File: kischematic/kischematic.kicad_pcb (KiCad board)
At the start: 2 copper layers, 26.7 x 50 mm, 104 parts, among them IC1 BlueNRG, IC10 128x64OLED, IC2 EFM32ZG108, IC3 BQ297xx, IC4 AAT3672IWO-4.2-1, IC5 TPS6223xx, IC6 APDS-9303, IC7 APDS-9303, IC8 BSD840NH6327XTSA1, IC9 MMA8653FC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

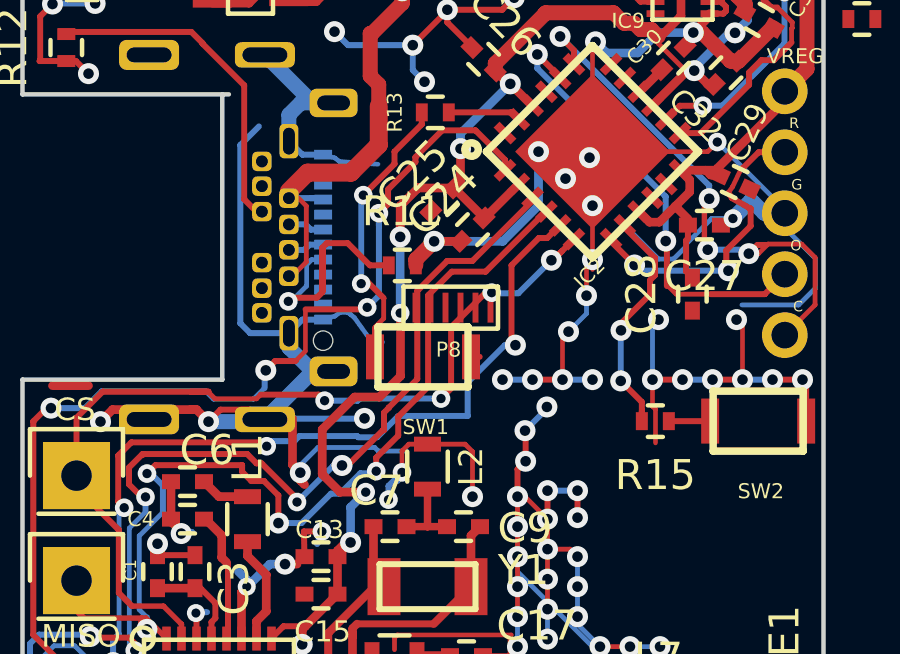
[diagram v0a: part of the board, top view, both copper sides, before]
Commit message: Some significant progress on display connector routing.
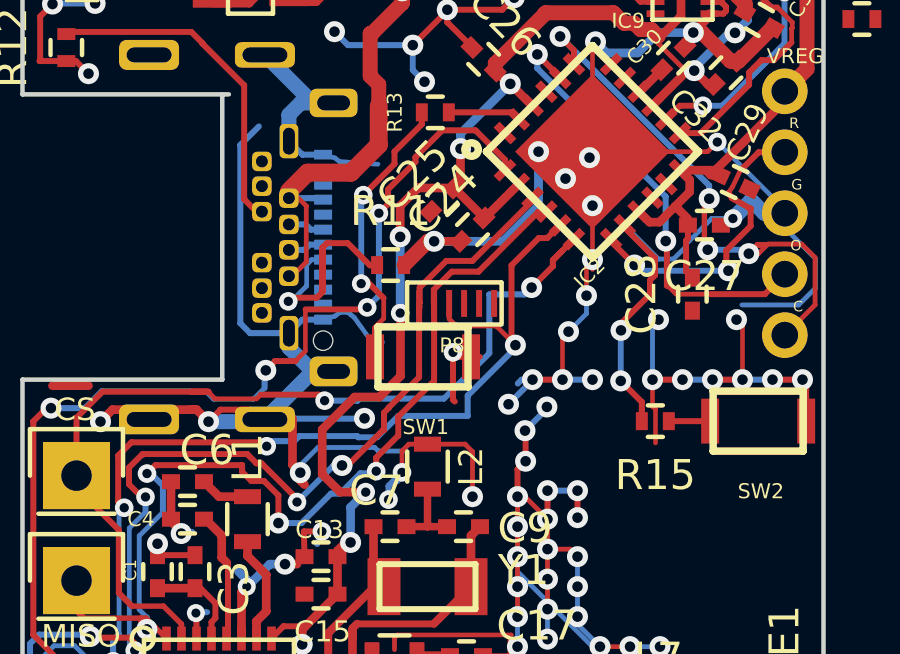
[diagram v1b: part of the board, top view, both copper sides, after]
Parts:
- moved R11 0.39 mm to (88.3, 49.8)
- moved P8 0.18 mm to (90.2, 51.1)
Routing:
- net GND: track 450.8 -> 454.1 mm, vias 161 -> 162
- net SPI_CLK: track 46.2 -> 49.1 mm
- net BNRG_SPI_CS: track 31.1 -> 31.2 mm, vias 4 -> 2

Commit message: Minor.
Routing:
- net GND: track 454.1 -> 451.7 mm, vias 162 -> 161
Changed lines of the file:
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@@
     (thickness 1.6)
     (drawings 22)
-    (tracks 1893)
+    (tracks 1890)
     (zones 0)
     (modules 104)
@@
   (segment (start 88.65 56.69) (end 88.2 57.14) (width 0.2) (layer B.Cu) (net 1))
   (segment (start 88.2 57.14) (end 88.2 57.6) (width 0.2) (layer B.Cu) (net 1))
-  (via (at 87.4 54.89) (size 0.7) (drill 0.35) (layers F.Cu B.Cu) (net 1))
-  (segment (start 85 54.9) (end 87.39 54.9) (width 0.2) (layer B.Cu) (net 1) (status 10))
-  (segment (start 87.39 54.9) (end 87.4 54.89) (width 0.2) (layer B.Cu) (net 1))
   (via (at 93 53.6) (size 0.7) (drill 0.35) (layers F.Cu B.Cu) (net 1))
   (segment (start 93 53.6) (end 94 53.6) (width 0.2) (layer F.Cu) (net 1))

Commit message: Some possible small steps of routing progress.
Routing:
- net VREG: track 202.1 -> 203.3 mm, vias 18 -> 20
- net BNRG_SPI_IRQ: track 48.9 -> 49.9 mm

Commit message: More routing tweaks.
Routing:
- net VREG: track 203.3 -> 203.9 mm, vias 20 -> 21
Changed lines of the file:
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@@
     (thickness 1.6)
     (drawings 22)
-    (tracks 1905)
+    (tracks 1911)
     (zones 0)
     (modules 104)
@@
   )
   (setup
-    (last_trace_width 0.16)
+    (last_trace_width 0.29)
     (user_trace_width 0.16)
     (user_trace_width 0.2)
@@
   (segment (start 94.92 44.11) (end 95.89 45.08) (width 0.2) (layer F.Cu) (net 1) (status 30))
   (segment (start 94 47) (end 95 48) (width 0.2) (layer F.Cu) (net 1) (status 30))
+  (segment (start 92.26 43.74) (end 92.26 43.7) (width 0.29) (layer B.Cu) (net 2))
+  (segment (start 92.26 43.7) (end 92.15 43.59) (width 0.29) (layer B.Cu) (net 2))
+  (segment (start 92.56 44) (end 92.2 43.64) (width 0.29) (layer B.Cu) (net 2))
+  (segment (start 92.15 43.59) (end 92.2 43.64) (width 0.29) (layer B.Cu) (net 2))
+  (segment (start 91.76 43.06) (end 92.15 42.67) (width 0.5) (layer F.Cu) (net 2))
+  (segment (start 92.15 42.67) (end 93.41 41.41) (width 0.5) (layer F.Cu) (net 2))
+  (segment (start 92.15 43.59) (end 92.15 42.67) (width 0.29) (layer B.Cu) (net 2))
+  (via (at 92.15 42.67) (size 0.62) (drill 0.31) (layers F.Cu B.Cu) (net 2))
+  (segment (start 93.002423 44.462043) (end 93.002423 44.442423) (width 0.29) (layer F.Cu) (net 2))
+  (segment (start 93.002423 44.442423) (end 92.56 44) (width 0.29) (layer F.Cu) (net 2))
+  (via (at 92.56 44) (size 0.62) (drill 0.31) (layers F.Cu B.Cu) (net 2))
   (via (at 90.65 45.45) (size 0.7) (drill 0.35) (layers F.Cu B.Cu) (net 2))
   (segment (start 90.65 45.45) (end 90.65 46.95) (width 0.29) (layer F.Cu) (net 2))
@@
   (segment (start 91.76 43.31) (end 91.76 43.06) (width 0.5) (layer F.Cu) (net 2) (status 30))
   (segment (start 93.41 41.41) (end 93.41 41.4) (width 0.5) (layer F.Cu) (net 2))
-  (segment (start 91.76 43.06) (end 93.41 41.41) (width 0.5) (layer F.Cu) (net 2) (status 10))
   (segment (start 96.05 41.72) (end 96.39 41.72) (width 0.5) (layer F.Cu) (net 2))
   (segment (start 93.41 41.4) (end 93.44 41.37) (width 0.5) (layer F.Cu) (net 2))
@@
   (segment (start 88 66.76) (end 88 67.2) (width 0.29) (layer F.Cu) (net 2))
   (segment (start 86.5 65.75) (end 86.99 65.75) (width 0.29) (layer F.Cu) (net 2))
-  (via (at 92.26 43.74) (size 0.7) (drill 0.35) (layers F.Cu B.Cu) (net 2))
   (segment (start 76.94 29.49) (end 76.8 29.63) (width 0.45) (layer F.Cu) (net 2))
   (segment (start 76.8 29.63) (end 76.8 31.175) (width 0.45) (layer F.Cu) (net 2))
@@
   (segment (start 98.938124 46.77756) (end 98.779282 46.618718) (width 0.29) (layer F.Cu) (net 2) (status 10))
   (via (at 99.75 42.04) (size 0.7) (drill 0.35) (layers F.Cu B.Cu) (net 2))
-  (segment (start 92.26 43.74) (end 92.19 43.74) (width 0.29) (layer F.Cu) (net 2))
-  (segment (start 92.19 43.74) (end 91.76 43.31) (width 0.29) (layer F.Cu) (net 2) (status 20))
   (segment (start 98.9 40.6) (end 99.55 40.6) (width 0.2) (layer F.Cu) (net 2) (status 30))
   (segment (start 99.55 40.6) (end 99.8 40.35) (width 0.2) (layer F.Cu) (net 2) (status 30))
@@
   (segment (start 97.916815 46.618718) (end 98.779282 46.618718) (width 0.29) (layer F.Cu) (net 2) (status 10))
   (segment (start 93.002423 44.462043) (end 92.982043 44.462043) (width 0.29) (layer F.Cu) (net 2) (status 30))
-  (segment (start 92.982043 44.462043) (end 92.26 43.74) (width 0.29) (layer F.Cu) (net 2) (status 10))
   (via (at 87.44 57.35) (size 0.62) (drill 0.31) (layers F.Cu B.Cu) (net 2))
   (segment (start 87.44 57.35) (end 86.59 57.35) (width 0.29) (layer F.Cu) (net 2))

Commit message: Some further routing tweaks.
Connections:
- IC2 pad 21: DISPLAY_CS -> MAINBUTTON
- IC2 pad 23: MAINBUTTON -> DISPLAY_CS
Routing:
- net DISPLAY_CS: track 0.01 -> 3.18 mm
- net MAINBUTTON: track 2.43 -> 4.07 mm
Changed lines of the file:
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@@
     (thickness 1.6)
     (drawings 22)
-    (tracks 1911)
+    (tracks 1920)
     (zones 0)
     (modules 104)
@@
   )
   (setup
-    (last_trace_width 0.29)
+    (last_trace_width 0.2)
     (user_trace_width 0.16)
     (user_trace_width 0.2)
@@
       (net 39 SWDIO))
     (pad 21 smd rect (at 0.325 -2.5 135) (size 0.8 0.28) (layers F.Cu F.Paste F.Mask)
-      (net 106 DISPLAY_CS))
+      (net 70 MAINBUTTON))
     (pad 22 smd rect (at -0.325 -2.5 135) (size 0.8 0.28) (layers F.Cu F.Paste F.Mask)
       (net 2 VREG))
     (pad 23 smd rect (at -0.975 -2.5 135) (size 0.8 0.28) (layers F.Cu F.Paste F.Mask)
-      (net 70 MAINBUTTON))
+      (net 106 DISPLAY_CS))
     (pad 24 smd rect (at -1.625 -2.499999 135) (size 0.8 0.28) (layers F.Cu F.Paste F.Mask)
       (net 105 DISPLAY_RESET))
@@
   (segment (start 94.92 44.11) (end 95.89 45.08) (width 0.2) (layer F.Cu) (net 1) (status 30))
   (segment (start 94 47) (end 95 48) (width 0.2) (layer F.Cu) (net 1) (status 30))
+  (via (at 92.58 44.05) (size 0.62) (drill 0.31) (layers F.Cu B.Cu) (net 2))
+  (segment (start 92.58 44.05) (end 92.58 44.02) (width 0.29) (layer B.Cu) (net 2))
+  (segment (start 92.58 44.02) (end 92.15 43.59) (width 0.29) (layer B.Cu) (net 2))
+  (segment (start 92.58 44.05) (end 92.59038 44.05) (width 0.29) (layer F.Cu) (net 2))
+  (segment (start 92.59038 44.05) (end 93.002423 44.462043) (width 0.29) (layer F.Cu) (net 2))
   (segment (start 92.26 43.74) (end 92.26 43.7) (width 0.29) (layer B.Cu) (net 2))
   (segment (start 92.26 43.7) (end 92.15 43.59) (width 0.29) (layer B.Cu) (net 2))
-  (segment (start 92.56 44) (end 92.2 43.64) (width 0.29) (layer B.Cu) (net 2))
-  (segment (start 92.15 43.59) (end 92.2 43.64) (width 0.29) (layer B.Cu) (net 2))
   (segment (start 91.76 43.06) (end 92.15 42.67) (width 0.5) (layer F.Cu) (net 2))
   (segment (start 92.15 42.67) (end 93.41 41.41) (width 0.5) (layer F.Cu) (net 2))
   (segment (start 92.15 43.59) (end 92.15 42.67) (width 0.29) (layer B.Cu) (net 2))
   (via (at 92.15 42.67) (size 0.62) (drill 0.31) (layers F.Cu B.Cu) (net 2))
-  (segment (start 93.002423 44.462043) (end 93.002423 44.442423) (width 0.29) (layer F.Cu) (net 2))
-  (segment (start 93.002423 44.442423) (end 92.56 44) (width 0.29) (layer F.Cu) (net 2))
-  (via (at 92.56 44) (size 0.62) (drill 0.31) (layers F.Cu B.Cu) (net 2))
   (via (at 90.65 45.45) (size 0.7) (drill 0.35) (layers F.Cu B.Cu) (net 2))
   (segment (start 90.65 45.45) (end 90.65 46.95) (width 0.29) (layer F.Cu) (net 2))
@@
   (segment (start 86.84 49.05) (end 86.15 49.05) (width 0.2) (layer F.Cu) (net 69))
   (segment (start 87.58 49.79) (end 86.84 49.05) (width 0.2) (layer F.Cu) (net 69))
-  (segment (start 92.521662 44.921662) (end 92.29 44.69) (width 0.2) (layer F.Cu) (net 70) (status 30))
-  (segment (start 92.29 44.69) (end 90.21 44.69) (width 0.2) (layer F.Cu) (net 70) (status 30))
-  (segment (start 92.542804 44.921662) (end 92.521662 44.921662) (width 0.2) (layer F.Cu) (net 70) (status 30))
+  (segment (start 92.46 43.37) (end 92.82962 43.37) (width 0.16) (layer F.Cu) (net 70))
+  (segment (start 92.82962 43.37) (end 93.462043 44.002423) (width 0.16) (layer F.Cu) (net 70))
+  (segment (start 91.79 44.04) (end 92.46 43.37) (width 0.16) (layer F.Cu) (net 70))
+  (segment (start 90.99 44.04) (end 91.79 44.04) (width 0.16) (layer F.Cu) (net 70))
+  (segment (start 90.34 44.69) (end 90.99 44.04) (width 0.2) (layer F.Cu) (net 70))
+  (segment (start 90.21 44.69) (end 90.34 44.69) (width 0.2) (layer F.Cu) (net 70))
+  (segment (start 93.452423 44.002423) (end 93.462043 44.002423) (width 0.2) (layer F.Cu) (net 70) (status 30))
   (segment (start 88.04 51.56) (end 88.04 50.9) (width 0.16) (layer F.Cu) (net 71))
   (segment (start 88.04 50.9) (end 88.05 50.89) (width 0.16) (layer F.Cu) (net 71))
@@
   (segment (start 83.9 40.7) (end 83.9 39.8) (width 0.29) (layer F.Cu) (net 102))
   (segment (start 83.95 39.75) (end 84.875 39.75) (width 0.29) (layer F.Cu) (net 102) (status 20))
-  (segment (start 93.452423 44.002423) (end 93.462043 44.002423) (width 0.2) (layer F.Cu) (net 106) (status 30))
+  (segment (start 91.34 44.84) (end 91.34 46.57) (width 0.2) (layer F.Cu) (net 106))
+  (segment (start 91.56 44.62) (end 91.34 44.84) (width 0.2) (layer F.Cu) (net 106))
+  (segment (start 92.26 44.62) (end 91.56 44.62) (width 0.2) (layer F.Cu) (net 106))
+  (segment (start 92.542804 44.902804) (end 92.26 44.62) (width 0.2) (layer F.Cu) (net 106))
+  (segment (start 92.542804 44.921662) (end 92.542804 44.902804) (width 0.2) (layer F.Cu) (net 106))
+  (segment (start 92.542804 44.921662) (end 92.521662 44.921662) (width 0.2) (layer F.Cu) (net 106) (status 30))
   (zone (net 1) (net_name GND) (layer F.Cu) (hatch edge 0.508)
     (connect_pads (clearance 0.18))

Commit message: More routing tweaks.
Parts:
- moved R13 0.30 mm to (89.8, 44.4)
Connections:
- IC2 pad 1: BNRG_SPI_IRQ -> DISPLAY_CS
- IC2 pad 23: DISPLAY_CS -> BNRG_SPI_IRQ
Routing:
- net DISPLAY_CS: track 3.18 -> 0.01 mm
- net BNRG_SPI_IRQ: track 49.9 -> 49.1 mm
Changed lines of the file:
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@@
     (thickness 1.6)
     (drawings 22)
-    (tracks 1920)
+    (tracks 1912)
     (zones 0)
     (modules 104)
@@
   )
   (setup
-    (last_trace_width 0.2)
+    (last_trace_width 0.16)
     (user_trace_width 0.16)
     (user_trace_width 0.2)
@@
       (net 2 VREG))
     (pad 23 smd rect (at -0.975 -2.5 135) (size 0.8 0.28) (layers F.Cu F.Paste F.Mask)
-      (net 106 DISPLAY_CS))
+      (net 28 BNRG_SPI_IRQ))
     (pad 24 smd rect (at -1.625 -2.499999 135) (size 0.8 0.28) (layers F.Cu F.Paste F.Mask)
       (net 105 DISPLAY_RESET))
@@
       (net 2 VREG))
     (pad 1 smd rect (at -2.499999 -1.625 45) (size 0.8 0.28) (layers F.Cu F.Paste F.Mask)
-      (net 28 BNRG_SPI_IRQ))
+      (net 106 DISPLAY_CS))
   )
   (module Capacitors_SMD:C_0402 (layer F.Cu)
@@
   )
   (module Resistors_SMD:R_0402 (layer F.Cu)
-    (at 89.76 44.69)
+    (at 89.79 44.39)
     (descr "Resistor SMD 0402, reflow soldering, Vishay (see dcrcw.pdf)")
     (tags "resistor 0402")
@@
   (segment (start 89.01 42.45) (end 89.01 43.28) (width 0.2) (layer B.Cu) (net 1))
   (segment (start 89.01 43.28) (end 89.4 43.67) (width 0.2) (layer B.Cu) (net 1))
-  (via (at 89.4 43.67) (size 0.7) (drill 0.35) (layers F.Cu B.Cu) (net 1))
+  (via (at 89.36 43.46) (size 0.7) (drill 0.35) (layers F.Cu B.Cu) (net 1))
   (segment (start 90.16 41.27) (end 90.16 41.3) (width 0.2) (layer F.Cu) (net 1))
   (segment (start 90.16 41.3) (end 89.01 42.45) (width 0.2) (layer F.Cu) (net 1))
@@
   (segment (start 94.92 44.11) (end 95.89 45.08) (width 0.2) (layer F.Cu) (net 1) (status 30))
   (segment (start 94 47) (end 95 48) (width 0.2) (layer F.Cu) (net 1) (status 30))
+  (via (at 90.65 45.52) (size 0.7) (drill 0.35) (layers F.Cu B.Cu) (net 2))
+  (segment (start 90.65 45.52) (end 90.65 46.95) (width 0.29) (layer F.Cu) (net 2))
+  (segment (start 90.65 46.95) (end 90.388909 47.211091) (width 0.29) (layer F.Cu) (net 2))
+  (segment (start 90.65 45.52) (end 90.65 45.35) (width 0.29) (layer B.Cu) (net 2))
+  (segment (start 90.65 45.35) (end 92.26 43.74) (width 0.29) (layer B.Cu) (net 2))
+  (segment (start 92.26 43.74) (end 92.26 43.7) (width 0.29) (layer B.Cu) (net 2))
+  (segment (start 92.26 43.7) (end 92.15 43.59) (width 0.29) (layer B.Cu) (net 2))
   (via (at 92.58 44.05) (size 0.62) (drill 0.31) (layers F.Cu B.Cu) (net 2))
   (segment (start 92.58 44.05) (end 92.58 44.02) (width 0.29) (layer B.Cu) (net 2))
@@
   (segment (start 92.58 44.05) (end 92.59038 44.05) (width 0.29) (layer F.Cu) (net 2))
   (segment (start 92.59038 44.05) (end 93.002423 44.462043) (width 0.29) (layer F.Cu) (net 2))
-  (segment (start 92.26 43.74) (end 92.26 43.7) (width 0.29) (layer B.Cu) (net 2))
-  (segment (start 92.26 43.7) (end 92.15 43.59) (width 0.29) (layer B.Cu) (net 2))
   (segment (start 91.76 43.06) (end 92.15 42.67) (width 0.5) (layer F.Cu) (net 2))
   (segment (start 92.15 42.67) (end 93.41 41.41) (width 0.5) (layer F.Cu) (net 2))
   (segment (start 92.15 43.59) (end 92.15 42.67) (width 0.29) (layer B.Cu) (net 2))
   (via (at 92.15 42.67) (size 0.62) (drill 0.31) (layers F.Cu B.Cu) (net 2))
-  (via (at 90.65 45.45) (size 0.7) (drill 0.35) (layers F.Cu B.Cu) (net 2))
-  (segment (start 90.65 45.45) (end 90.65 46.95) (width 0.29) (layer F.Cu) (net 2))
-  (segment (start 90.65 46.95) (end 90.388909 47.211091) (width 0.29) (layer F.Cu) (net 2))
-  (segment (start 90.65 45.45) (end 90.65 45.35) (width 0.29) (layer B.Cu) (net 2))
-  (segment (start 90.65 45.35) (end 92.26 43.74) (width 0.29) (layer B.Cu) (net 2))
   (via (at 88.59 48.54) (size 0.62) (drill 0.31) (layers F.Cu B.Cu) (net 2))
   (segment (start 88.59 48.54) (end 88.59 51.38) (width 0.29) (layer B.Cu) (net 2))
@@
   (segment (start 93 64.8) (end 93 66.25) (width 1.2) (layer F.Cu) (net 25) (status 30))
   (segment (start 89.15 62.8) (end 90.25 62.8) (width 0.29) (layer F.Cu) (net 26) (status 30))
-  (segment (start 91.33 47.55) (end 90.86 48.02) (width 0.16) (layer F.Cu) (net 28))
-  (segment (start 90.86 48.02) (end 90.42 48.02) (width 0.16) (layer F.Cu) (net 28))
-  (segment (start 90.42 48.02) (end 89.74 47.34) (width 0.16) (layer F.Cu) (net 28))
-  (segment (start 89.74 47.34) (end 89.54 47.34) (width 0.16) (layer F.Cu) (net 28))
-  (segment (start 89.54 47.34) (end 88.98 47.9) (width 0.16) (layer F.Cu) (net 28))
-  (segment (start 88.98 47.9) (end 88.98 48.14) (width 0.16) (layer F.Cu) (net 28))
-  (segment (start 88.98 48.14) (end 89.14 48.3) (width 0.16) (layer F.Cu) (net 28))
-  (segment (start 87.880813 48.740813) (end 87.880813 48.052123) (width 0.16) (layer F.Cu) (net 28))
-  (segment (start 89.14 48.3) (end 89.14 48.78) (width 0.16) (layer F.Cu) (net 28))
-  (segment (start 89.14 48.78) (end 88.75 49.17) (width 0.16) (layer F.Cu) (net 28))
-  (segment (start 88.75 49.17) (end 88.31 49.17) (width 0.16) (layer F.Cu) (net 28))
-  (segment (start 88.31 49.17) (end 87.880813 48.740813) (width 0.16) (layer F.Cu) (net 28))
-  (segment (start 91.33 47.36) (end 91.33 47.55) (width 0.2) (layer F.Cu) (net 28))
-  (segment (start 92.071282 46.618718) (end 91.33 47.36) (width 0.2) (layer F.Cu) (net 28))
-  (segment (start 92.083185 46.618718) (end 92.071282 46.618718) (width 0.2) (layer F.Cu) (net 28))
+  (segment (start 92.542804 44.921662) (end 92.542804 44.912804) (width 0.16) (layer F.Cu) (net 28))
+  (segment (start 92.542804 44.912804) (end 92.17 44.54) (width 0.16) (layer F.Cu) (net 28))
+  (segment (start 92.17 44.54) (end 90.98 44.54) (width 0.16) (layer F.Cu) (net 28))
+  (segment (start 90.98 44.54) (end 90.58 44.94) (width 0.16) (layer F.Cu) (net 28))
+  (segment (start 88.87 46.34) (end 88.87 46.71) (width 0.16) (layer F.Cu) (net 28))
+  (segment (start 90.58 44.94) (end 90.27 44.94) (width 0.16) (layer F.Cu) (net 28))
+  (segment (start 90.27 44.94) (end 88.87 46.34) (width 0.16) (layer F.Cu) (net 28))
+  (segment (start 88.87 46.71) (end 87.880813 47.699187) (width 0.16) (layer F.Cu) (net 28))
+  (segment (start 87.880813 47.699187) (end 87.880813 48.052123) (width 0.16) (layer F.Cu) (net 28))
   (segment (start 87.880813 48.490529) (end 87.880813 48.052123) (width 0.2) (layer B.Cu) (net 28))
   (segment (start 85.1 52.98) (end 85.11 52.98) (width 0.16) (layer F.Cu) (net 28))
@@
   (segment (start 84.07 53.33) (end 84.11 53.29) (width 0.2) (layer B.Cu) (net 28))
   (segment (start 80.01 64.02) (end 78.72 64.02) (width 0.29) (layer F.Cu) (net 28) (status 30))
+  (segment (start 92.542804 44.921662) (end 92.542804 44.902804) (width 0.2) (layer F.Cu) (net 28))
+  (segment (start 92.542804 44.921662) (end 92.521662 44.921662) (width 0.2) (layer F.Cu) (net 28) (status 30))
   (via (at 92.97 50.53) (size 0.7) (drill 0.35) (layers F.Cu B.Cu) (net 29))
   (segment (start 92.97 50.53) (end 92.74 50.76) (width 0.2) (layer B.Cu) (net 29))
@@
   (segment (start 86.84 49.05) (end 86.15 49.05) (width 0.2) (layer F.Cu) (net 69))
   (segment (start 87.58 49.79) (end 86.84 49.05) (width 0.2) (layer F.Cu) (net 69))
+  (segment (start 90.99 44.04) (end 90.59 44.04) (width 0.2) (layer F.Cu) (net 70))
+  (segment (start 90.59 44.04) (end 90.24 44.39) (width 0.2) (layer F.Cu) (net 70))
   (segment (start 92.46 43.37) (end 92.82962 43.37) (width 0.16) (layer F.Cu) (net 70))
   (segment (start 92.82962 43.37) (end 93.462043 44.002423) (width 0.16) (layer F.Cu) (net 70))
   (segment (start 91.79 44.04) (end 92.46 43.37) (width 0.16) (layer F.Cu) (net 70))
   (segment (start 90.99 44.04) (end 91.79 44.04) (width 0.16) (layer F.Cu) (net 70))
-  (segment (start 90.34 44.69) (end 90.99 44.04) (width 0.2) (layer F.Cu) (net 70))
-  (segment (start 90.21 44.69) (end 90.34 44.69) (width 0.2) (layer F.Cu) (net 70))
   (segment (start 93.452423 44.002423) (end 93.462043 44.002423) (width 0.2) (layer F.Cu) (net 70) (status 30))
+  (segment (start 89.31 45.09) (end 89.31 44.42) (width 0.2) (layer F.Cu) (net 71))
+  (segment (start 89.31 44.42) (end 89.34 44.39) (width 0.2) (layer F.Cu) (net 71))
   (segment (start 88.04 51.56) (end 88.04 50.9) (width 0.16) (layer F.Cu) (net 71))
   (segment (start 88.04 50.9) (end 88.05 50.89) (width 0.16) (layer F.Cu) (net 71))
@@
   (segment (start 87.75 52.84) (end 87.75 51.88) (width 0.2) (layer F.Cu) (net 71) (status 10))
   (segment (start 88.05 50.89) (end 88.03 50.87) (width 0.16) (layer F.Cu) (net 71))
-  (segment (start 89.31 44.69) (end 89.31 45.09) (width 0.2) (layer F.Cu) (net 71) (status 10))
   (segment (start 89.31 45.09) (end 88.4 46) (width 0.2) (layer F.Cu) (net 71))
   (segment (start 88.4 46) (end 88.4 46.41) (width 0.2) (layer F.Cu) (net 71))
@@
   (segment (start 83.9 40.7) (end 83.9 39.8) (width 0.29) (layer F.Cu) (net 102))
   (segment (start 83.95 39.75) (end 84.875 39.75) (width 0.29) (layer F.Cu) (net 102) (status 20))
-  (segment (start 91.34 44.84) (end 91.34 46.57) (width 0.2) (layer F.Cu) (net 106))
-  (segment (start 91.56 44.62) (end 91.34 44.84) (width 0.2) (layer F.Cu) (net 106))
-  (segment (start 92.26 44.62) (end 91.56 44.62) (width 0.2) (layer F.Cu) (net 106))
-  (segment (start 92.542804 44.902804) (end 92.26 44.62) (width 0.2) (layer F.Cu) (net 106))
-  (segment (start 92.542804 44.921662) (end 92.542804 44.902804) (width 0.2) (layer F.Cu) (net 106))
-  (segment (start 92.542804 44.921662) (end 92.521662 44.921662) (width 0.2) (layer F.Cu) (net 106) (status 30))
+  (segment (start 92.083185 46.618718) (end 92.071282 46.618718) (width 0.2) (layer F.Cu) (net 106))
   (zone (net 1) (net_name GND) (layer F.Cu) (hatch edge 0.508)
     (connect_pads (clearance 0.18))
